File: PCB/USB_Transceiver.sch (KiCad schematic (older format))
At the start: 9 parts

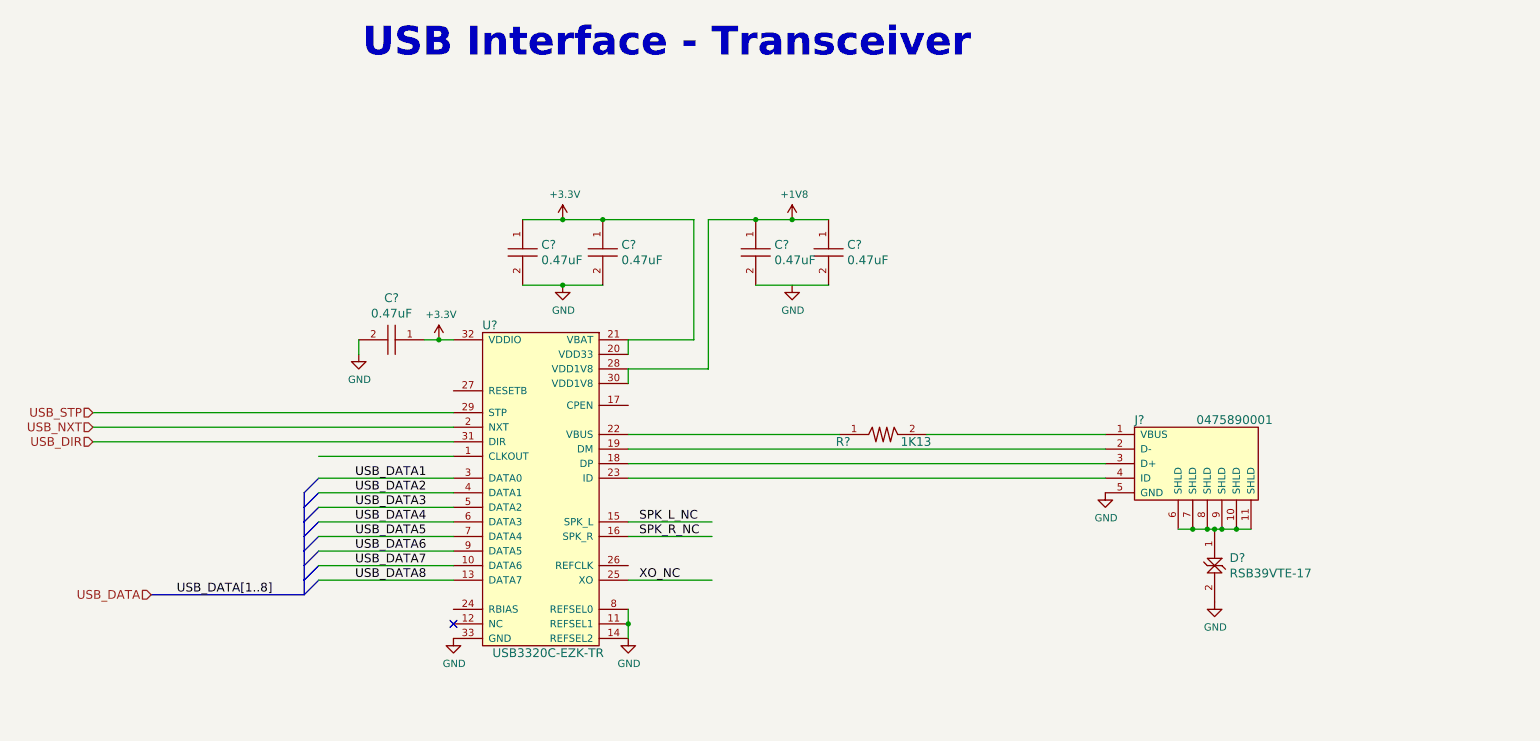
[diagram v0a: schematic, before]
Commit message: USB PHY
USB PHY/Transceiver schematic implemented. ZyncMV can host USB
peripherals and utilize them.
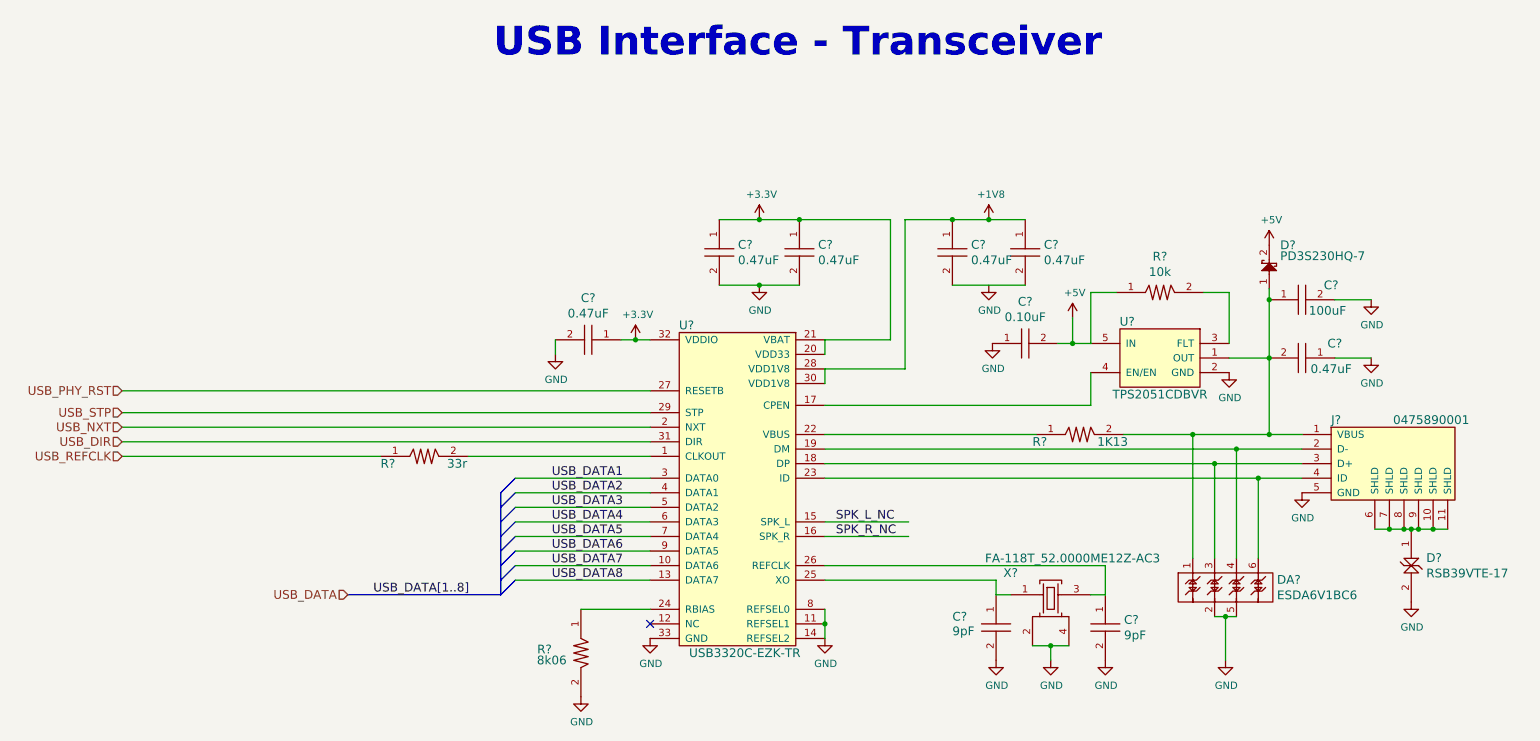
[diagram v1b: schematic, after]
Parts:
- added C?: CL05A104JO5NNNC, PCB_Footprints:C0402, symbol CL05A104JO5NNNC
- added C? (x2): CL05C090CB5NNNC, PCB_Footprints:C0402, symbol CL05C090CB5NNNC
- added C?: GRM31CR60J107ME39K, PCB_Footprints:C1206, symbol GRM31CR60J107ME39K
- added C?: CL05A474KQ5NNNC, PCB_Footprints:C0402, symbol CL05A474KQ5NNNC
- added D?: PD3S230HQ-7, PCB_Footprints:BAT20JFILM, symbol PD3S230HQ-7
- added DA?: ESDA6V1BC6, PCB_Footprints:ESDA6V1BC6, symbol ESDA6V1BC6
- added R?: RC1005F103CS, PCB_Footprints:R0402, symbol RC1005F103CS
- added R?: RC0402FR-0733RL, PCB_Footprints:R0402, symbol RC0402FR-0733RL
- added R?: RC0402FR-078K06L, PCB_Footprints:R0402, symbol RC0402FR-078K06L
- added U?: TPS2051CDBVR, PCB_Footprints:TPS2051CDBVR, symbol TPS2051CDBVR
- added X?: FA-118T_52.0000ME12Z-AC3, PCB_Footprints:FA-118T_52.0000ME12Z-AC3, symbol FA-118T_52.0000ME12Z-AC3
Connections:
- net labels added: +5V, USB_PHY_RST, USB_REFCLK
- net labels removed: XO_NC
- wire segments 46 -> 62
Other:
- moved on the sheet: C?, D?, J?, R?, U?
